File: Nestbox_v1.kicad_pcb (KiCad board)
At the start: 2 copper layers, 100 x 91 mm, 447 parts, among them Q1 SFH 3605, Q2 SFH 3605, SW1 SMD-BUTTON_2P-3.0X2.5X1.2+0.4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, U1 MSP430FR5969, U2 CR95HF, U3 TPS630250RNC, U4 RN2483, Y1 Crystal, Y2 ABM11-142-27.120MHz

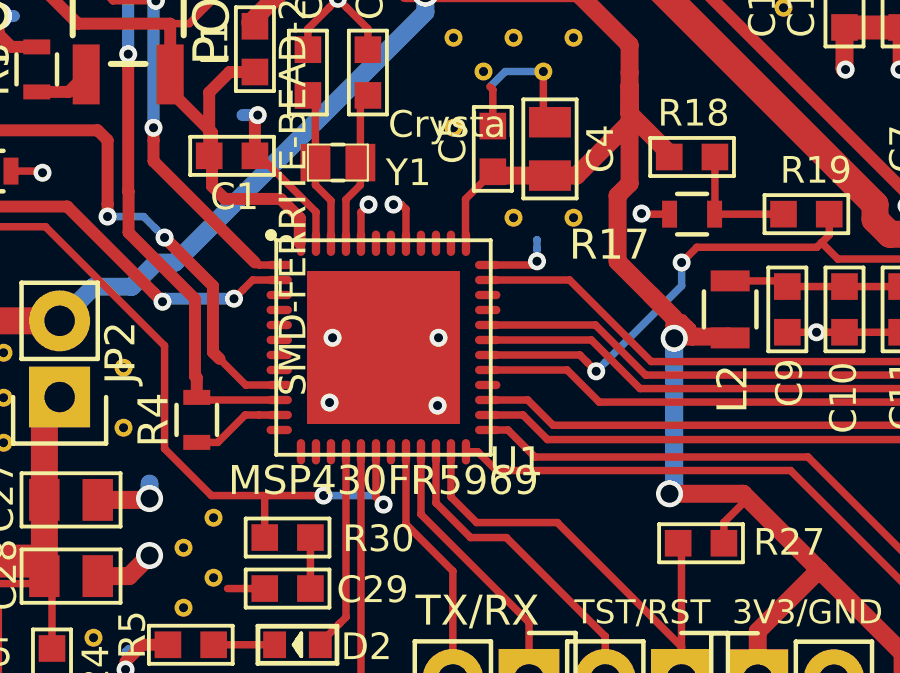
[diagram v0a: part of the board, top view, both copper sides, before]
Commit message: corrected solder mask expansion and generated paste gerber file
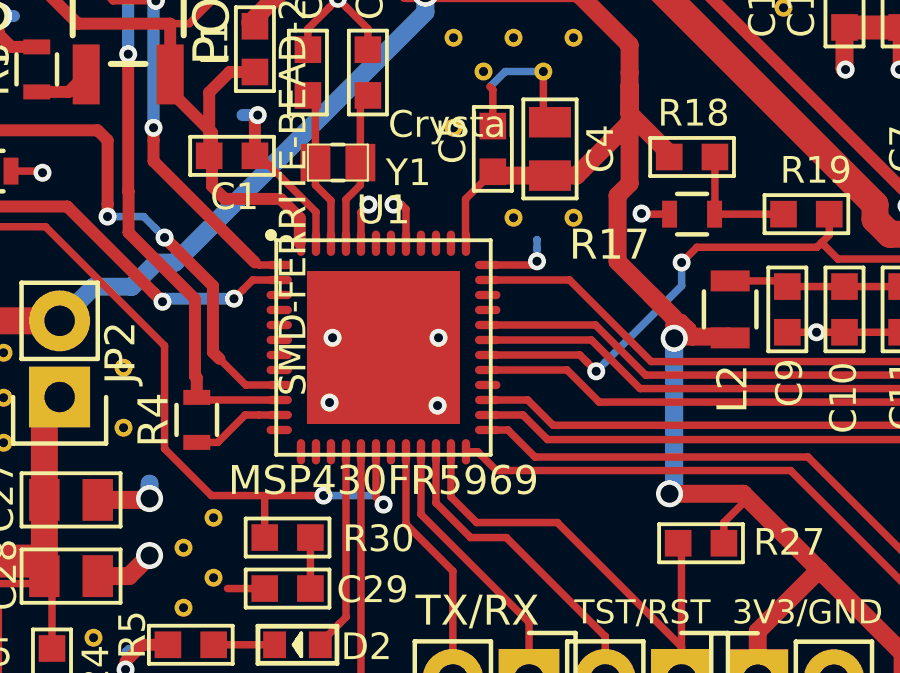
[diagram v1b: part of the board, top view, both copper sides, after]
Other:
- rule pad_to_mask_clearance: 0.2 -> 0.01

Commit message: updated pcb v1 (?)
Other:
- board text added: "warning: pad 1 here is pad 2 in datasheet!"
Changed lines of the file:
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@@
-(kicad_pcb (version 4) (host pcbnew 4.0.4-stable)
+(kicad_pcb (version 20170123) (host pcbnew "(2017-06-12 revision 19d5cc754)-master")
   (general
     (links 570)
     (no_connects 4)
-    (area 92.809524 51.584999 201.053999 149.277101)
+    (area 92.734524 49.145 222.55 149.315201)
     (thickness 1.6)
-    (drawings 16)
+    (drawings 17)
     (tracks 921)
     (zones 0)
@@
       (hpglpenspeed 20)
       (hpglpendiameter 15)
-      (hpglpenoverlay 2)
       (psnegative false)
       (psa4output false)
@@
   (module Octanis3:RN2483 (layer F.Cu)
     (at 158.336 123 270)
-    (fp_text reference U4 (at 1.398 -28.364 540) (layer F.SilkS)
+    (fp_text reference U4 (at 1.398 -28.364 180) (layer F.SilkS)
       (effects (font (thickness 0.15)))
     )
@@
     (tags 0402)
     (attr smd)
-    (fp_text reference C19 (at -2.647 -0.073 540) (layer F.SilkS)
+    (fp_text reference C19 (at -2.647 -0.073 180) (layer F.SilkS)
       (effects (font (size 0.889 0.889) (thickness 0.1016)))
     )
-    (fp_text value CERAMIC-47PF-50V-5%-NP0_0402_ (at -1.2065 0.508 540) (layer F.SilkS)
+    (fp_text value CERAMIC-47PF-50V-5%-NP0_0402_ (at -1.2065 0.508 180) (layer F.SilkS)
       (effects (font (size 0.635 0.635) (thickness 0.0762)))
     )
@@
     (tags 0402)
     (attr smd)
-    (fp_text reference C22 (at 2.647 0.023 360) (layer F.SilkS)
+    (fp_text reference C22 (at 2.647 0.023) (layer F.SilkS)
       (effects (font (size 0.889 0.889) (thickness 0.1016)))
     )
-    (fp_text value CERAMIC-47PF-50V-5%-NP0_0402_ (at -1.2065 0.508 360) (layer F.SilkS)
+    (fp_text value CERAMIC-47PF-50V-5%-NP0_0402_ (at -1.2065 0.508) (layer F.SilkS)
       (effects (font (size 0.635 0.635) (thickness 0.0762)))
     )
@@
     (tags "resistor 0603")
     (attr smd)
-    (fp_text reference R15 (at 0.05 -5.532 450) (layer F.SilkS)
+    (fp_text reference R15 (at 0.05 -5.532 90) (layer F.SilkS)
       (effects (font (size 1 1) (thickness 0.15)))
     )
@@
     (at 147.287 126.785 270)
     (descr "<b>32-lead very thin fine pitch quad flat no-lead package (5 x 5)</b><p>\nSource: <a href=\"http://www.st.com/stonline/products/literature/ds/14771/stm8s105c4.pdf\"> Data sheet </a>")
-    (fp_text reference U2 (at -3.185 -3.013 360) (layer F.SilkS)
+    (fp_text reference U2 (at -3.185 -3.013) (layer F.SilkS)
       (effects (font (size 1 1) (thickness 0.15)))
     )
@@
   (module Octanis3:RNC0014A (layer F.Cu)
     (at 108.171 136.945 270)
-    (fp_text reference U3 (at -1.545 3.771 360) (layer F.SilkS)
+    (fp_text reference U3 (at -1.545 3.771) (layer F.SilkS)
       (effects (font (size 1.2065 1.2065) (thickness 0.0762)) (justify left bottom))
     )
@@
     (at 137.762 124.88 270)
     (attr smd)
-    (fp_text reference R19 (at -1.4605 -0.3175 360) (layer F.SilkS)
+    (fp_text reference R19 (at -1.4605 -0.3175) (layer F.SilkS)
       (effects (font (size 0.889 0.889) (thickness 0.1016)))
     )
-    (fp_text value SMD-RES-3.3K-1%-1_10W_0603_ (at 1.11506 -0.29972 360) (layer F.Fab)
+    (fp_text value SMD-RES-3.3K-1%-1_10W_0603_ (at 1.11506 -0.29972) (layer F.Fab)
       (effects (font (size 0.635 0.635) (thickness 0.0762)))
     )
@@
     (at 133.952 122.975 270)
     (attr smd)
-    (fp_text reference R18 (at -1.4605 -0.048 360) (layer F.SilkS)
+    (fp_text reference R18 (at -1.4605 -0.048) (layer F.SilkS)
       (effects (font (size 0.889 0.889) (thickness 0.1016)))
     )
-    (fp_text value SMD-RES-0R-5%-1_10W_0603_ (at 1.11506 -0.29972 360) (layer F.Fab)
+    (fp_text value SMD-RES-0R-5%-1_10W_0603_ (at 1.11506 -0.29972) (layer F.Fab)
       (effects (font (size 0.635 0.635) (thickness 0.0762)))
     )
@@
     (tags 0603)
     (attr smd)
-    (fp_text reference C16 (at 3.337 0.095 450) (layer F.SilkS)
+    (fp_text reference C16 (at 3.337 0.095 90) (layer F.SilkS)
       (effects (font (size 0.889 0.889) (thickness 0.1016)))
     )
@@
     (at 177.386 120.054 270)
     (attr smd)
-    (fp_text reference R26 (at -1.654 -0.114 360) (layer F.SilkS)
+    (fp_text reference R26 (at -1.654 -0.114) (layer F.SilkS)
       (effects (font (size 0.889 0.889) (thickness 0.1016)))
     )
-    (fp_text value SMD-RES-10K-1%-1_10W_0603_ (at 1.11506 -0.29972 360) (layer F.Fab)
+    (fp_text value SMD-RES-10K-1%-1_10W_0603_ (at 1.11506 -0.29972) (layer F.Fab)
       (effects (font (size 0.635 0.635) (thickness 0.0762)))
     )
@@
     (descr "Through hole socket strip")
     (tags "socket strip")
-    (fp_text reference PB2 (at 1.07 -2.38 450) (layer F.SilkS)
+    (fp_text reference PB2 (at 1.07 -2.38 90) (layer F.SilkS)
       (effects (font (size 1 1) (thickness 0.15)))
     )
@@
     (descr "Through hole socket strip")
     (tags "socket strip")
-    (fp_text reference PB1 (at 1.202 -2.3 450) (layer F.SilkS)
+    (fp_text reference PB1 (at 1.202 -2.3 90) (layer F.SilkS)
       (effects (font (size 1 1) (thickness 0.15)))
     )
@@
     (at 117.242 139.234 270)
     (attr smd)
-    (fp_text reference R5 (at -0.334 1.942 450) (layer F.SilkS)
+    (fp_text reference R5 (at -0.334 1.942 90) (layer F.SilkS)
       (effects (font (size 0.889 0.889) (thickness 0.1016)))
     )
-    (fp_text value SMD-RES-1K-5%-1_10W_0603_ (at 1.11506 -0.29972 360) (layer F.Fab)
+    (fp_text value SMD-RES-1K-5%-1_10W_0603_ (at 1.11506 -0.29972) (layer F.Fab)
       (effects (font (size 0.635 0.635) (thickness 0.0762)))
     )
@@
     (at 117.242 141.012 270)
     (attr smd)
-    (fp_text reference R6 (at 0.088 1.842 450) (layer F.SilkS)
+    (fp_text reference R6 (at 0.088 1.842 90) (layer F.SilkS)
       (effects (font (size 0.889 0.889) (thickness 0.1016)))
     )
-    (fp_text value SMD-RES-1K-5%-1_10W_0603_ (at 1.11506 -0.29972 360) (layer F.Fab)
+    (fp_text value SMD-RES-1K-5%-1_10W_0603_ (at 1.11506 -0.29972) (layer F.Fab)
       (effects (font (size 0.635 0.635) (thickness 0.0762)))
     )
@@
     (tags 0603)
     (attr smd)
-    (fp_text reference C29 (at 0.04 -2.832 360) (layer F.SilkS)
+    (fp_text reference C29 (at 0.04 -2.832) (layer F.SilkS)
       (effects (font (size 0.889 0.889) (thickness 0.1016)))
     )
-    (fp_text value CERAMIC-100NF-50V-10%-X7R_0603_ (at -1.27 0.635 360) (layer F.Fab)
+    (fp_text value CERAMIC-100NF-50V-10%-X7R_0603_ (at -1.27 0.635) (layer F.Fab)
       (effects (font (size 0.635 0.635) (thickness 0.0762)))
     )
@@
   (module Octanis3:NFC_ANTENNA_CIRC (layer F.Cu)
     (at 146.65 104.47 270)
-    (fp_text reference ant1 (at 0.94 -4.748 360) (layer F.SilkS)
+    (fp_text reference ant1 (at 0.94 -4.748) (layer F.SilkS)
       (effects (font (thickness 0.15)))
     )
@@
       (net 2 GND))
   )
+  (gr_text "warning: pad 1 here is pad 2 in datasheet!\n" (at 197.4 50.3) (layer F.Fab)
+    (effects (font (size 1.5 1.5) (thickness 0.3)))
+  )
   (gr_text "Octanis 3: Digital Nestbox PCB v1.0\n\nnestbox.octanis.org" (at 147 93) (layer F.SilkS)
